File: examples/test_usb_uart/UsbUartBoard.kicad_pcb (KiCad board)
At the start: 2 copper layers, 78 x 87 mm, 14 parts, among them J1 COM-15111 (Sparkfun), U1 CP2102 (Silicon Labs), U2 ESDA5V3L (STMicroelectronics), U3 Duck, U4 LeadFree, U5 IdDots4

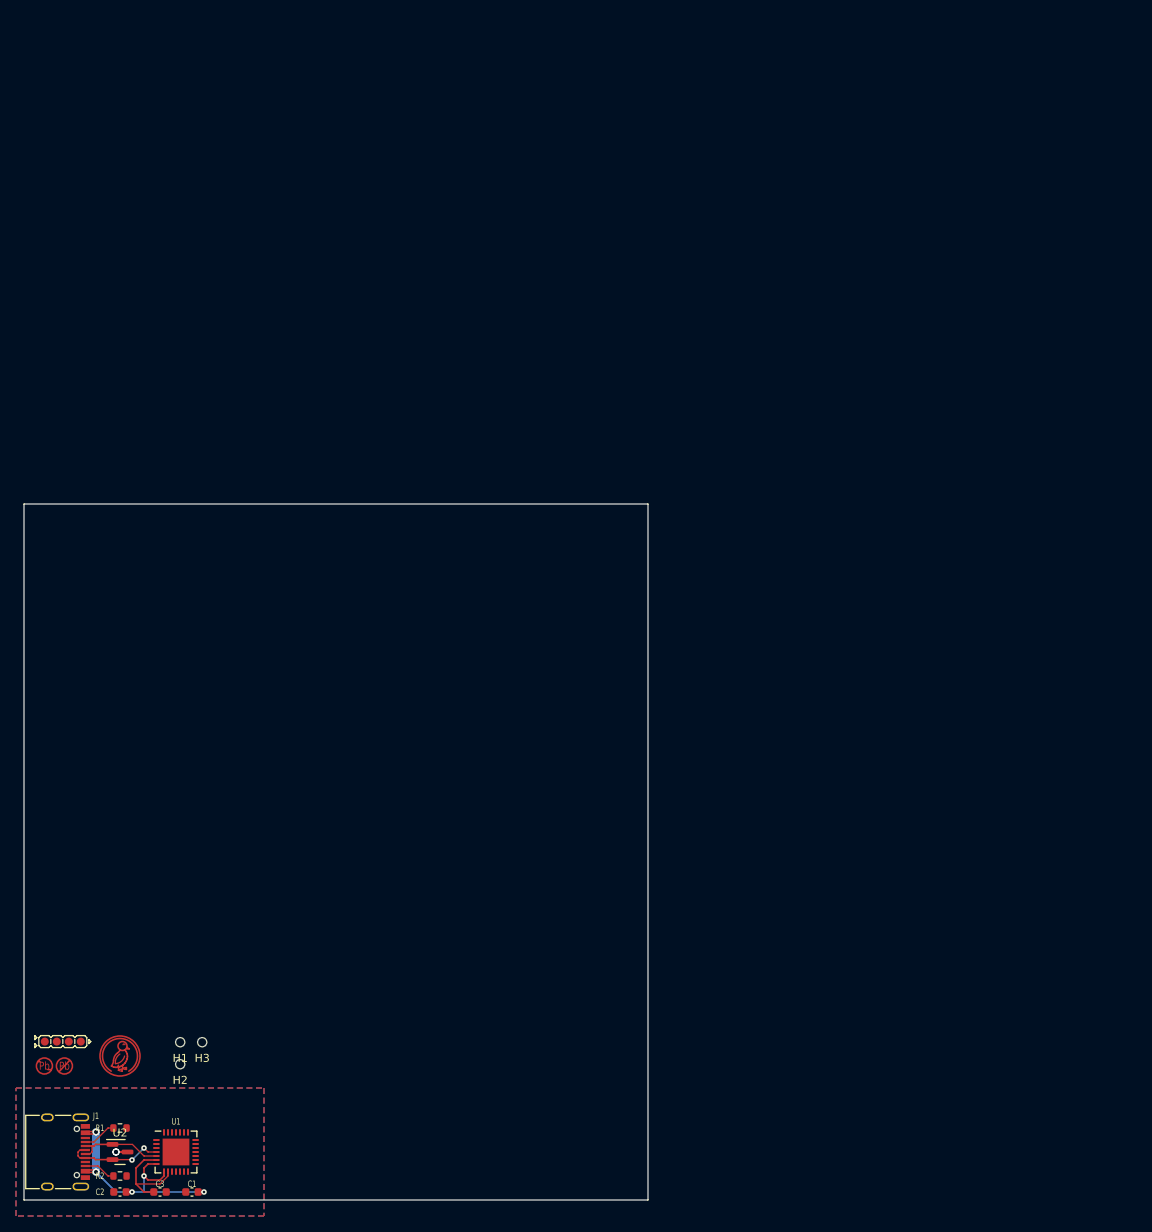
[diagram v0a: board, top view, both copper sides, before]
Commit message: usb uart board done
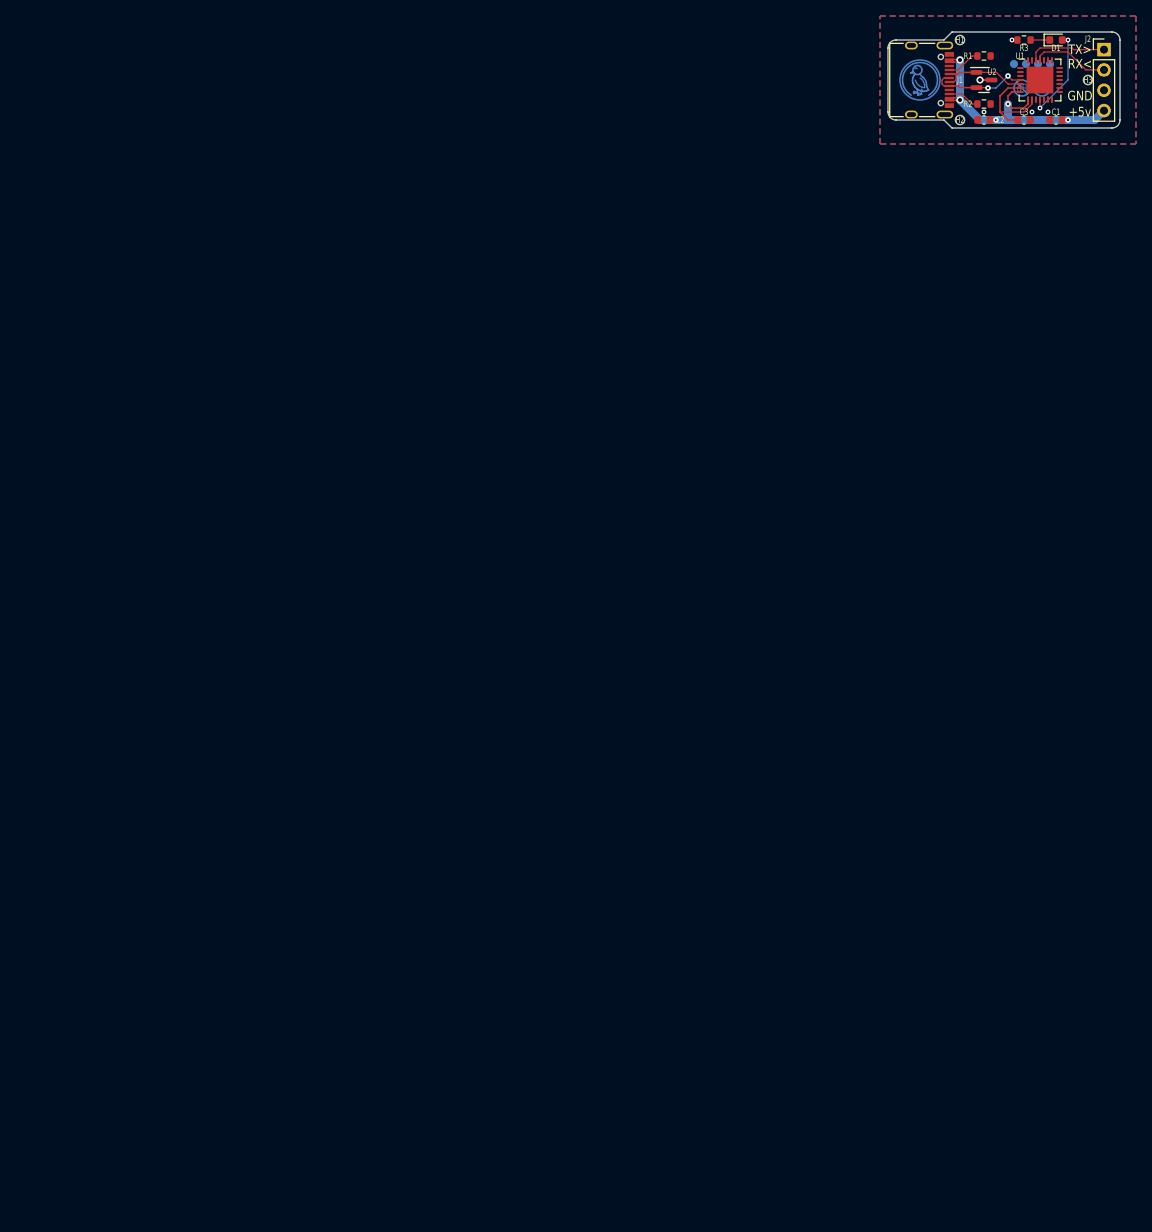
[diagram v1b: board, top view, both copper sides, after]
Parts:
- added D1: KT-0603R (Hubei KENTO Elec) - Red 615~630nm 1.9~2.2V 0603 L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, LED_SMD:LED_0603_1608Metric, F.Cu at (155.0, 43.0)
- added J2: PinHeader2.54 1x4 (Generic), Connector_PinHeader_2.54mm:PinHeader_1x04_P2.54mm_Vertical, F.Cu at (161.0, 44.2)
- added R3: , Resistor_SMD:R_0603_1608Metric, F.Cu at (151.0, 43.0)
- U3, U4, U5: moved to B.Cu
- moved U4 172.9 mm to (152.0, 49.0), turned to 180 degrees
- moved C1 172.1 mm to (155.0, 53.0)
- moved C2 172.1 mm to (146.0, 53.0)
- moved C3 172.1 mm to (151.0, 53.0)
- moved J1 172.1 mm to (138.0, 48.0)
- moved R1 172.1 mm to (146.0, 45.0)
- moved R2 172.1 mm to (146.0, 51.0)
- moved U1 172.1 mm to (153.0, 48.0)
- moved U2 172.1 mm to (146.0, 48.0)
- moved U5 172.1 mm to (152.0, 46.0), turned to 180 degrees
- moved H3 163.5 mm to (159.0, 48.0)
- moved H1 158.7 mm to (143.0, 43.0)
- moved U3 157.7 mm to (138.0, 48.0), turned to 180 degrees
- moved H2 153.1 mm to (143.0, 53.0)
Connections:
- U1 pad 11: (no net) -> usbconv.nsuspend
- U1 pad 12: (no net) -> usbconv.suspend
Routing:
- net vusb: track 34.8 -> 48.8 mm
- net usbconv.nsuspend: track 0.00 -> 11.7 mm, vias 0 -> 2
- net usbconv.uart.tx: track 0.00 -> 9.84 mm
- net usbconv.uart.rx: track 0.00 -> 9.68 mm
- net led.res.a: track 0.00 -> 2.39 mm
- net gnd: track 2.88 -> 3.55 mm, vias 2 -> 5
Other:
- board size 78 x 87 mm -> 29 x 12 mm
- board text added: "+5v"
- board text added: "GND"
- board text added: "RX<"
- board text added: "TX>"

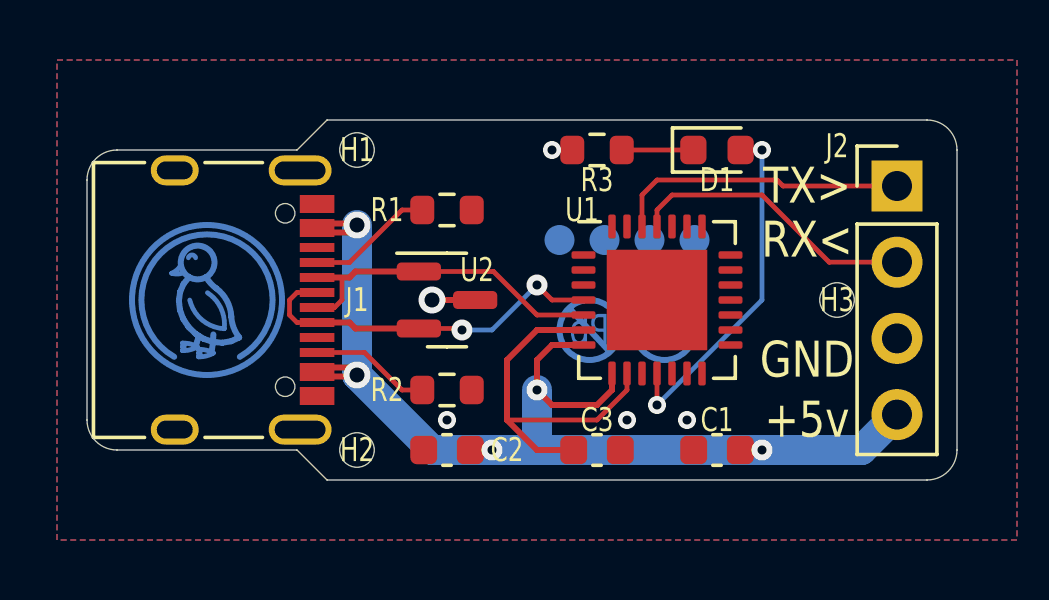
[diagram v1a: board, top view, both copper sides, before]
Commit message: refdes for panelization
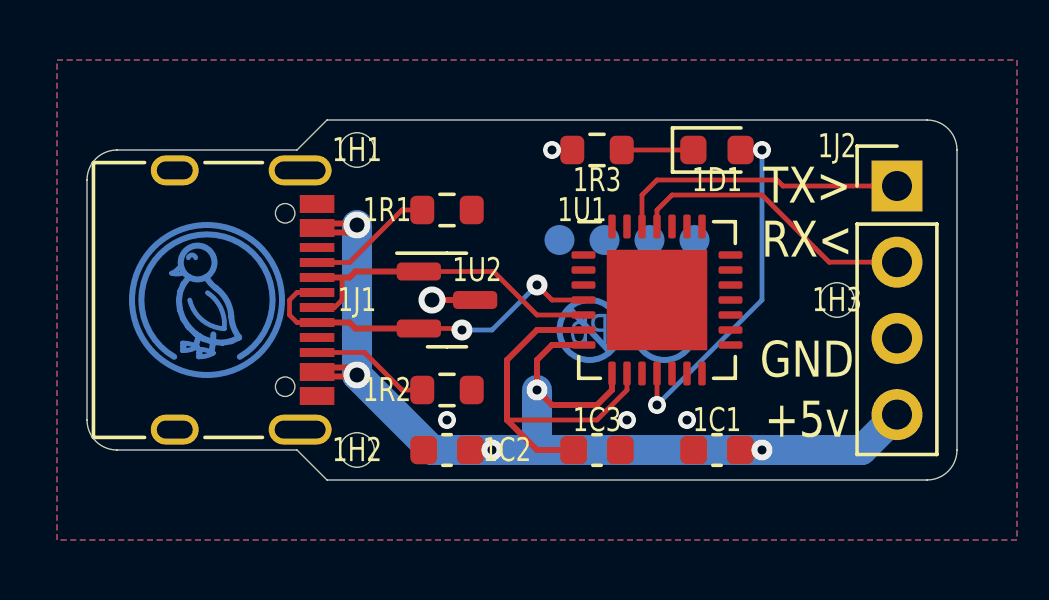
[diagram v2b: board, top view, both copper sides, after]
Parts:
- renumbered C1 to 1C1, C2 to 1C2, C3 to 1C3, D1 to 1D1, H1 to 1H1, H2 to 1H2, H3 to 1H3, J1 to 1J1, J2 to 1J2, R1 to 1R1, R2 to 1R2, R3 to 1R3, U1 to 1U1, U2 to 1U2, U3 to 1U3, U4 to 1U4, U5 to 1U5

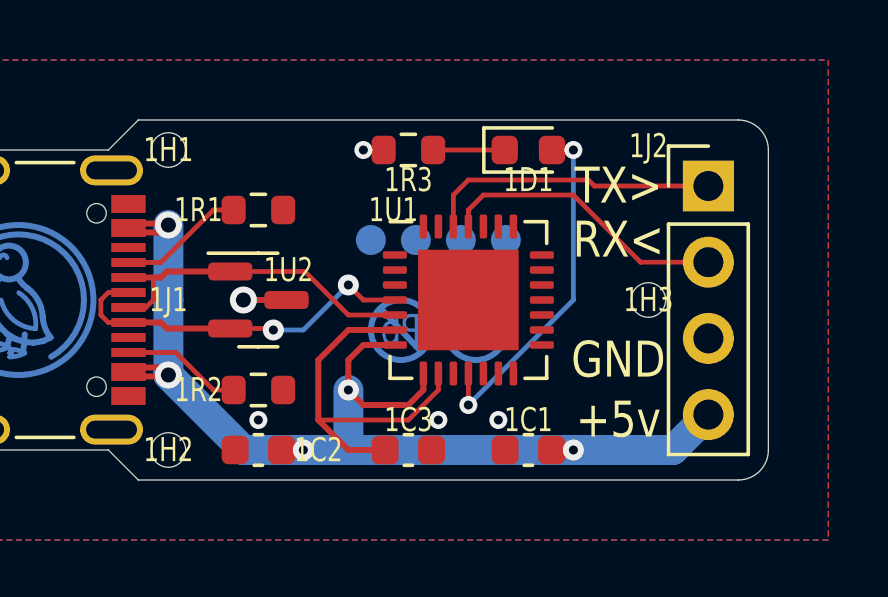
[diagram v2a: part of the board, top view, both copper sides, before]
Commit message: properly ground EP
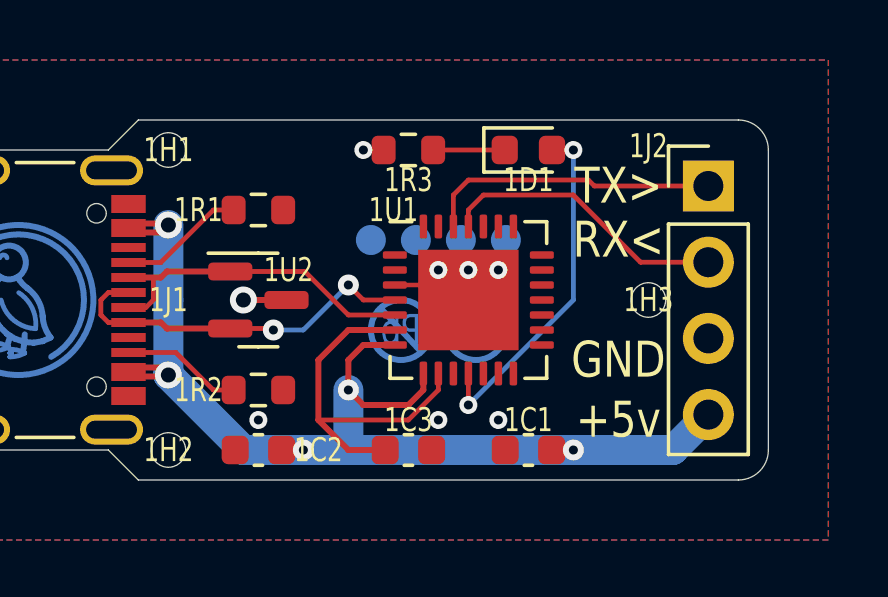
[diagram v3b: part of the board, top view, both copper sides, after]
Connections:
- 1U1 pad 29: (no net) -> gnd
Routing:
- net gnd: track 3.55 -> 6.21 mm, vias 5 -> 8
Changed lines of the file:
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@@
     (pad "28" smd roundrect (at -1.5 -2.45) (size 0.25 0.8) (layers "F.Cu" "F.Paste" "F.Mask") (roundrect_rratio 0.25)
       (net 13 "usbconv.dtr"))
-    (pad "29" smd rect (at 0 0) (size 3.35 3.35) (layers "F.Cu" "F.Mask"))
+    (pad "29" smd rect (at 0 0) (size 3.35 3.35) (layers "F.Cu" "F.Mask")
+      (net 1 "gnd"))
     (model "${KICAD6_3DMODEL_DIR}/Package_DFN_QFN.3dshapes/QFN-28-1EP_5x5mm_P0.5mm_EP3.35x3.35mm.wrl"
       (offset (xyz 0 0 0))
@@
     (fp_arc (start -0.573812 -0.957555) (mid 0.159981 -0.670103) (end 0.575946 -0.000734) (layer "B.Cu") (width 0.16))
     (fp_arc (start 0.286757 -1.643905) (mid 0.02807 -1.671353) (end -0.213115 -1.768832) (layer "B.Cu") (width 0.16))
-    (fp_arc (start 0.763205 0.913443) (mid 0.969127 0.866754) (end 1.178844 0.891296) (layer "B.Cu") (width 0.16))
+    (fp_arc (start 0.763205 0.913443) (mid 0.969127 0.866755) (end 1.178844 0.891296) (layer "B.Cu") (width 0.16))
     (fp_arc (start 0.320058 -1.56145) (mid 0.561228 -1.658966) (end 0.819911 -1.686455) (layer "B.Cu") (width 0.16))
     (fp_arc (start -0.303506 0.391461) (mid -0.661618 -0.021387) (end -0.809366 -0.547561) (layer "B.Cu") (width 0.2))
@@
     (fp_arc (start -0.303506 0.391461) (mid -0.117368 0.560252) (end 0.03125 0.762861) (layer "B.Cu") (width 0.2))
     (fp_arc (start -1.072198 -1.25) (mid -0.886856 -0.918958) (end -0.809364 -0.547562) (layer "B.Cu") (width 0.2))
-    (fp_arc (start 0.869178 1.169286) (mid 1.000174 1.003685) (end 1.178836 0.891151) (layer "B.Cu") (width 0.16))
+    (fp_arc (start 0.869178 1.169286) (mid 1.000175 1.003685) (end 1.178836 0.891151) (layer "B.Cu") (width 0.16))
     (fp_arc (start 1.093749 -1.89443) (mid 0.000001 2.187499) (end -1.09375 -1.894429) (layer "B.Cu") (width 0.2))
     (fp_circle (center 0.3125 1.25) (end 0.875 1.25) (layer "B.Cu") (width 0.2) (fill none))
@@
   )
   (segment (start 146.9375 48) (end 145.5 48) (width 0.2) (layer "F.Cu") (net 1))
+  (segment (start 152.5 47.5) (end 153 48) (width 0.15) (layer "F.Cu") (net 1))
+  (segment (start 150.55 47.5) (end 152.5 47.5) (width 0.15) (layer "F.Cu") (net 1))
   (segment (start 146.9375 48) (end 145.5 48) (width 0.2) (layer "F.Cu") (net 1))
   (segment (start 150.175 43) (end 149.5 43) (width 0.16) (layer "F.Cu") (net 1))
+  (via (at 154 47) (size 0.6) (drill 0.3) (layers "F.Cu" "B.Cu") (net 1))
+  (via (at 153 47) (size 0.6) (drill 0.3) (layers "F.Cu" "B.Cu") (net 1))
   (via (at 152 52) (size 0.6) (drill 0.3) (layers "F.Cu" "B.Cu") (net 1))
   (via (at 149.5 43) (size 0.6) (drill 0.3) (layers "F.Cu" "B.Cu") (net 1))
@@
   (via (at 145.5 48) (size 0.9) (drill 0.5) (layers "F.Cu" "B.Cu") (net 1))
   (via (at 154 52) (size 0.6) (drill 0.3) (layers "F.Cu" "B.Cu") (net 1))
+  (via (at 152 47) (size 0.6) (drill 0.3) (layers "F.Cu" "B.Cu") (net 1))
   (segment (start 149 48.5) (end 150.55 48.5) (width 0.16) (layer "F.Cu") (net 2))
   (segment (start 142.5 47.25) (end 142.75 47.25) (width 0.16) (layer "F.Cu") (net 2))

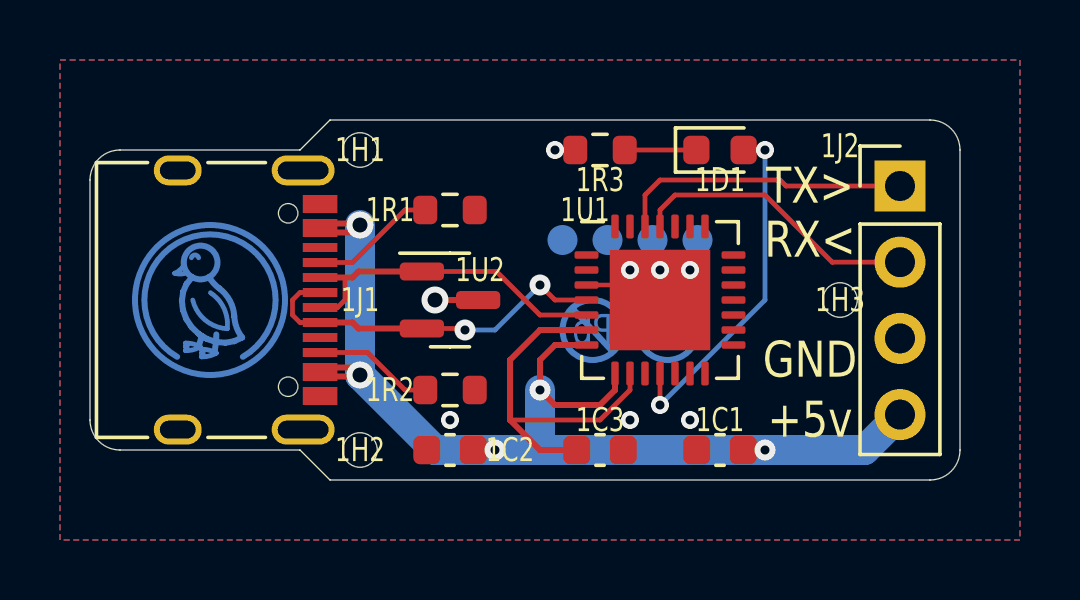
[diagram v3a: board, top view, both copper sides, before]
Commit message: leds and protection diodes
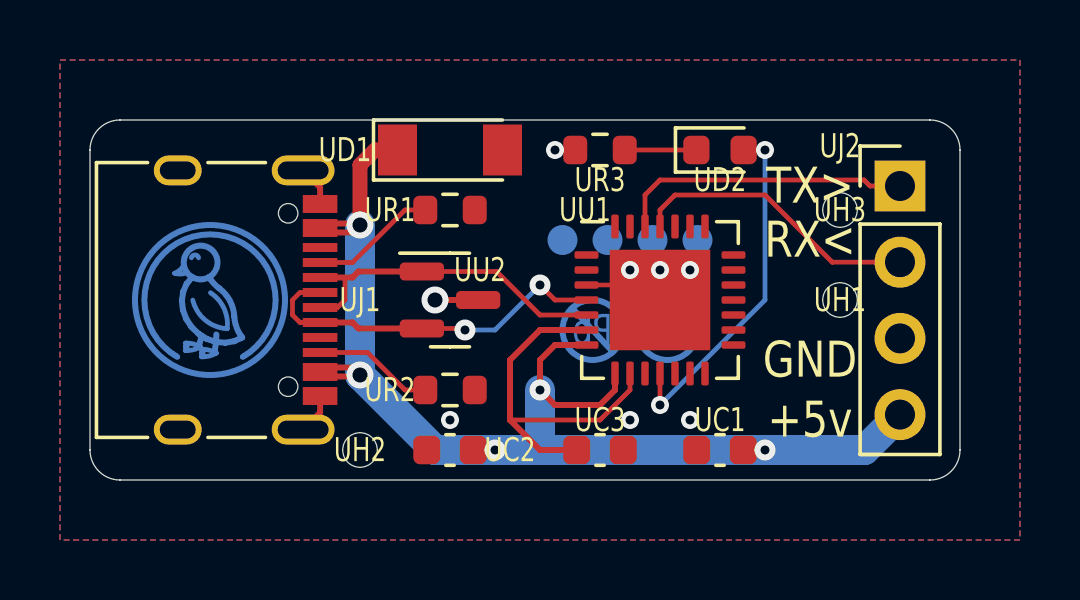
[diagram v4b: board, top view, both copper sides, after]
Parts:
- added UD1: , Diode_SMD:D_MiniMELF, F.Cu at (146.0, 43.0)
- moved UH1 16.8 mm to (159.0, 48.0)
- moved UH3 3.00 mm to (159.0, 45.0)
- renumbered 1C1 to UC1, 1C2 to UC2, 1C3 to UC3, 1D1 to UD2, 1H1 to UH1, 1H2 to UH2, 1H3 to UH3, 1J1 to UJ1, 1J2 to UJ2, 1R1 to UR1, 1R2 to UR2, 1R3 to UR3, 1U1 to UU1, 1U2 to UU2, 1U3 to UU3, 1U4 to UU4, 1U5 to UU5
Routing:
- net vusb: track 48.8 -> 52.2 mm
- net gnd: track 6.21 -> 8.62 mm
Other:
- outline, holes or cut-outs redrawn
